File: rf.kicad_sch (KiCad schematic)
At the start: 25 parts, among them J1 Coil, Q1 J177, U1 MCP6022, U2 MCP6022, U3 74HCT4053

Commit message: ESP module pins
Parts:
- renumbered J1 to L1
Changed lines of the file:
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@@
 		(dnp no)
 		(fields_autoplaced yes)
-		(property "Reference" "J1"
+		(property "Reference" "L1"
 			(at 50.8 74.93 0)
 			(show_name no)
@@
 			(project "pcsk225_ntp"
 				(path "/ece5592d-c78f-4d56-a72a-26347184f54b/c523a75c-6254-41cb-8170-0ba25fada1a2"
-					(reference "J1")
+					(reference "L1")
 					(unit 1)
 				)

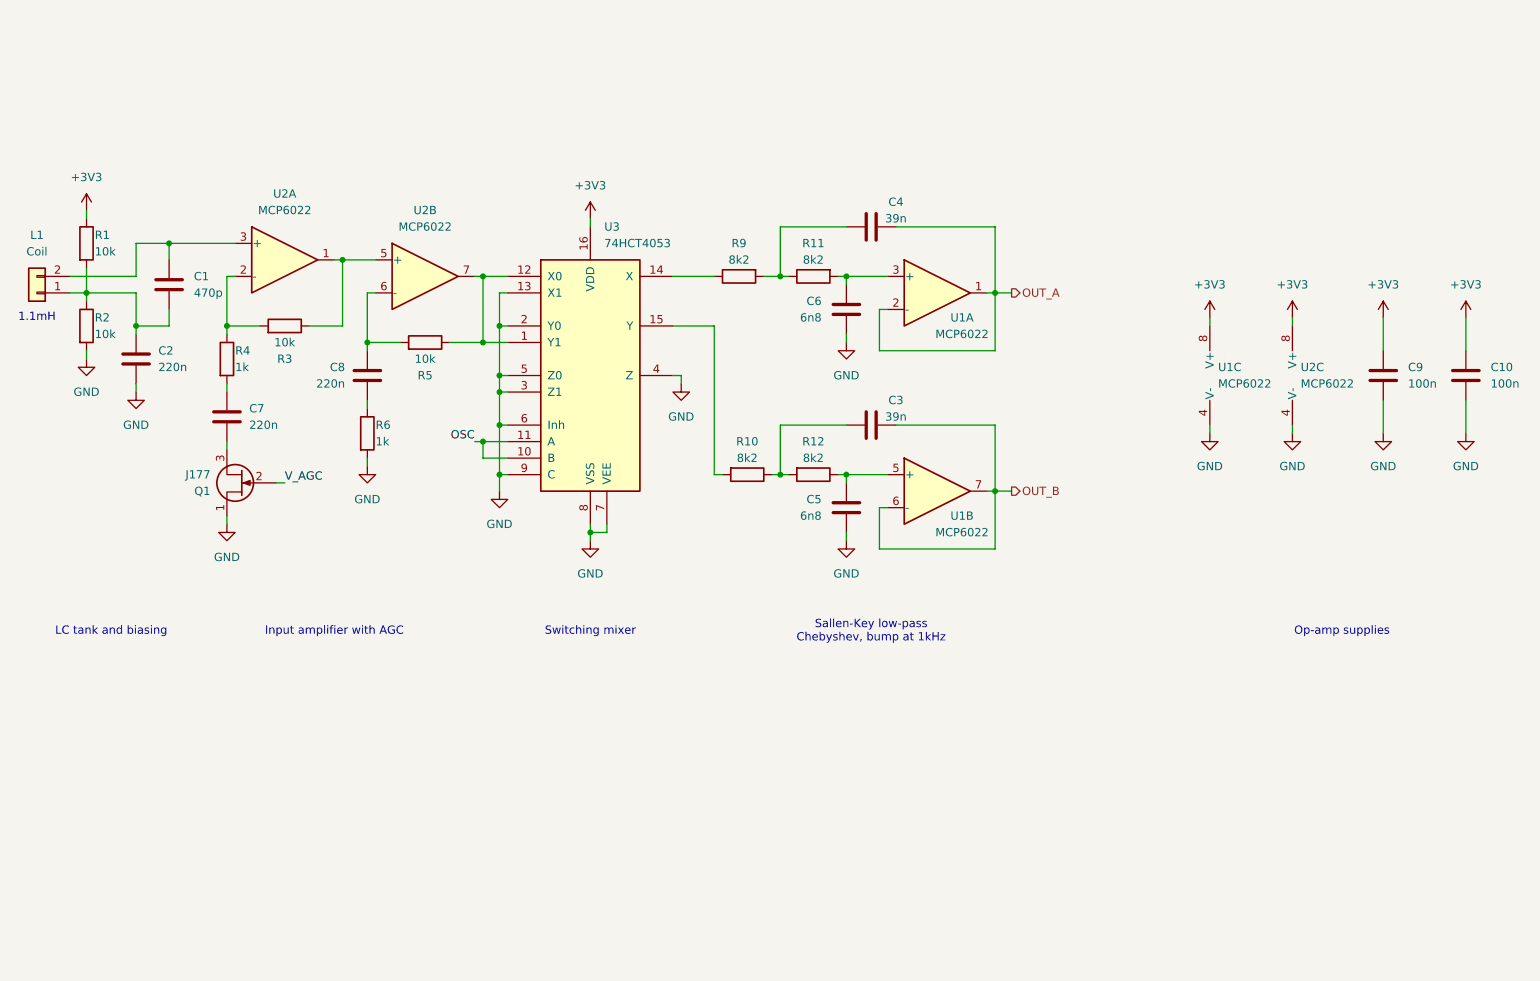
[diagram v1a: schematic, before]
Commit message: update
- fixed what the switching mixer sees when the input is "disabled" - tied to 1/2*3.3V instead of GND
- added another J-FET transistor to the AGC loop
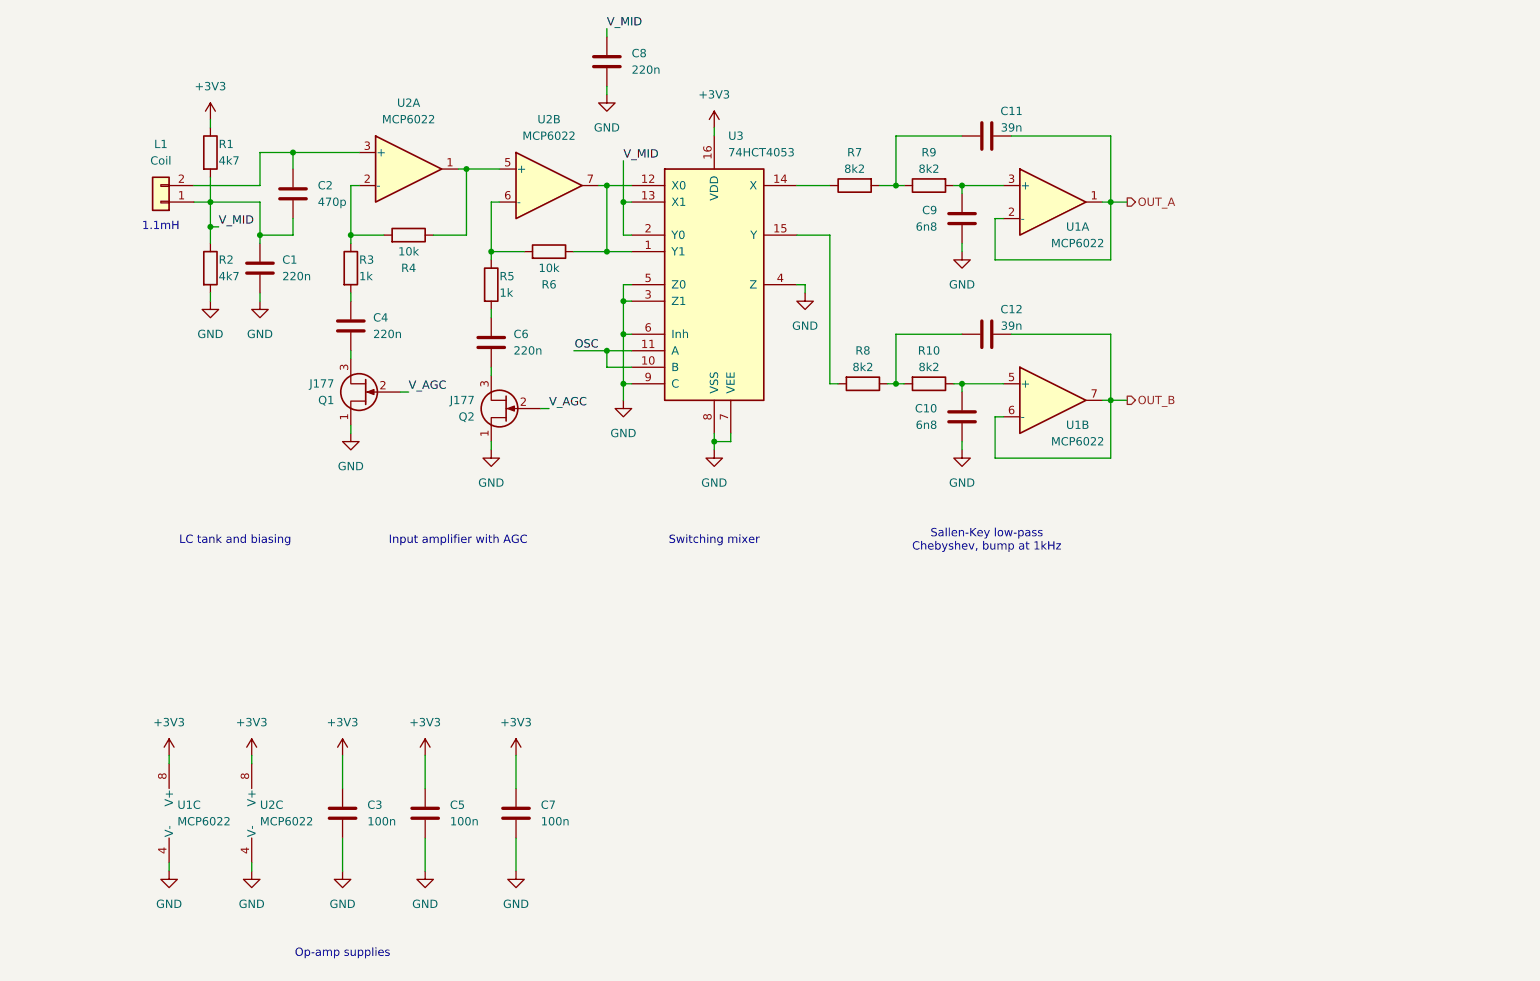
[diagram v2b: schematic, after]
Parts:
- added C7: 100n, symbol Device:C
- added C8: 220n, symbol Device:C
- added Q2: J177, symbol Device:Q_NJFET_DGS
- R1, R2: value 10k -> 4k7
- renumbered C2 to C1, C5 to C10, C4 to C11, C3 to C12, C1 to C2, C9 to C3, C7 to C4, C10 to C5, C8 to C6, C6 to C9, R12 to R10, R4 to R3, R3 to R4, R6 to R5, R5 to R6, R9 to R7, R10 to R8, R11 to R9
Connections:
- net +3V3: now also C7.2
- net GND: now also C7.1, C8.2, Q2.1 (D); no longer R5.2, U3.13 (X1), U3.2 (Y0)
- net V_AGC: now also Q2.2 (G)
- net at R6.2, U2.6 (-): now also R5.1; no longer C6.2
- net at C6.1: now also Q2.3 (S); no longer R5.1
- net V_MID: now reaches C1.2, C2.1, L1.1 (Pin_1), R1.2, R2.1
- net V_MID: now also U3.13 (X1), U3.2 (Y0), C8.1
- new net: C6.2, R5.2
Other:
- company: (none) -> Wojciech Kaczmarski SP5WWP
- moved on the sheet: C1, C10, C11, C12, C2, C3, C4, C5, C6, C9, L1, Q1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

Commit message: update
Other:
- note added: "Op-amp supplies Decoupling caps"
- note removed: "Op-amp supplies"
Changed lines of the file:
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@@
 		)
 	)
-	(text "Op-amp supplies"
+	(text "Op-amp supplies\nDecoupling caps"
 		(exclude_from_sim no)
 		(at 97.79 185.42 0)
